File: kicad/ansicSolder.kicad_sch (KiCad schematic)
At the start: 56 parts, among them J1 AudioJack4, J2 AudioJack4, J3 Conn_01x02_Socket, SW1 SW_Push, SW10 SW_Push, SW11 SW_Push, SW12 SW_Push, SW13 SW_Push, SW14 SW_Push, SW15 SW_Push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

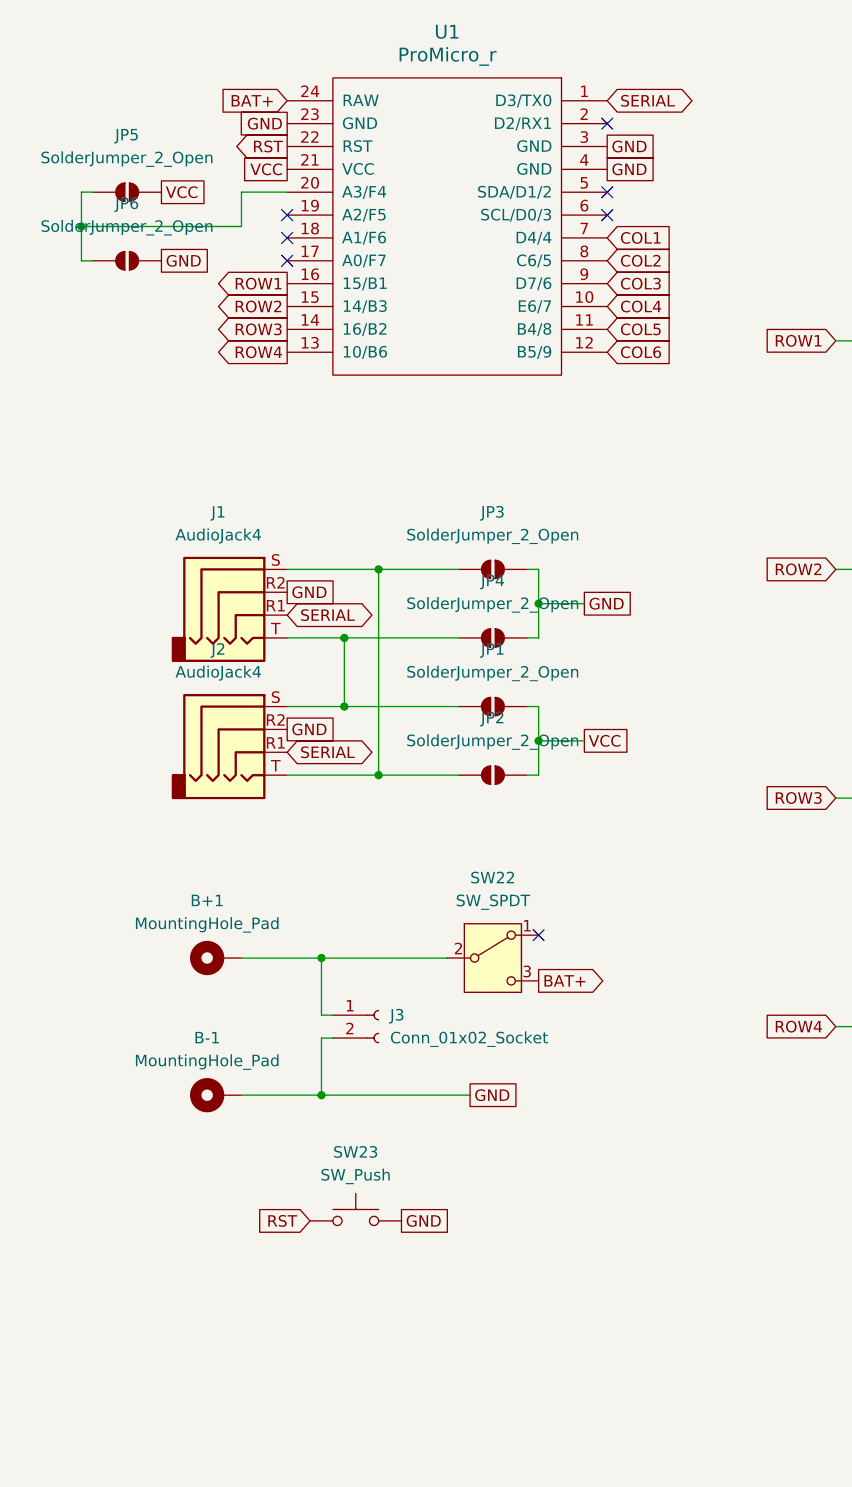
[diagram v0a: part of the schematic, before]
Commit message: edit for more readable schema
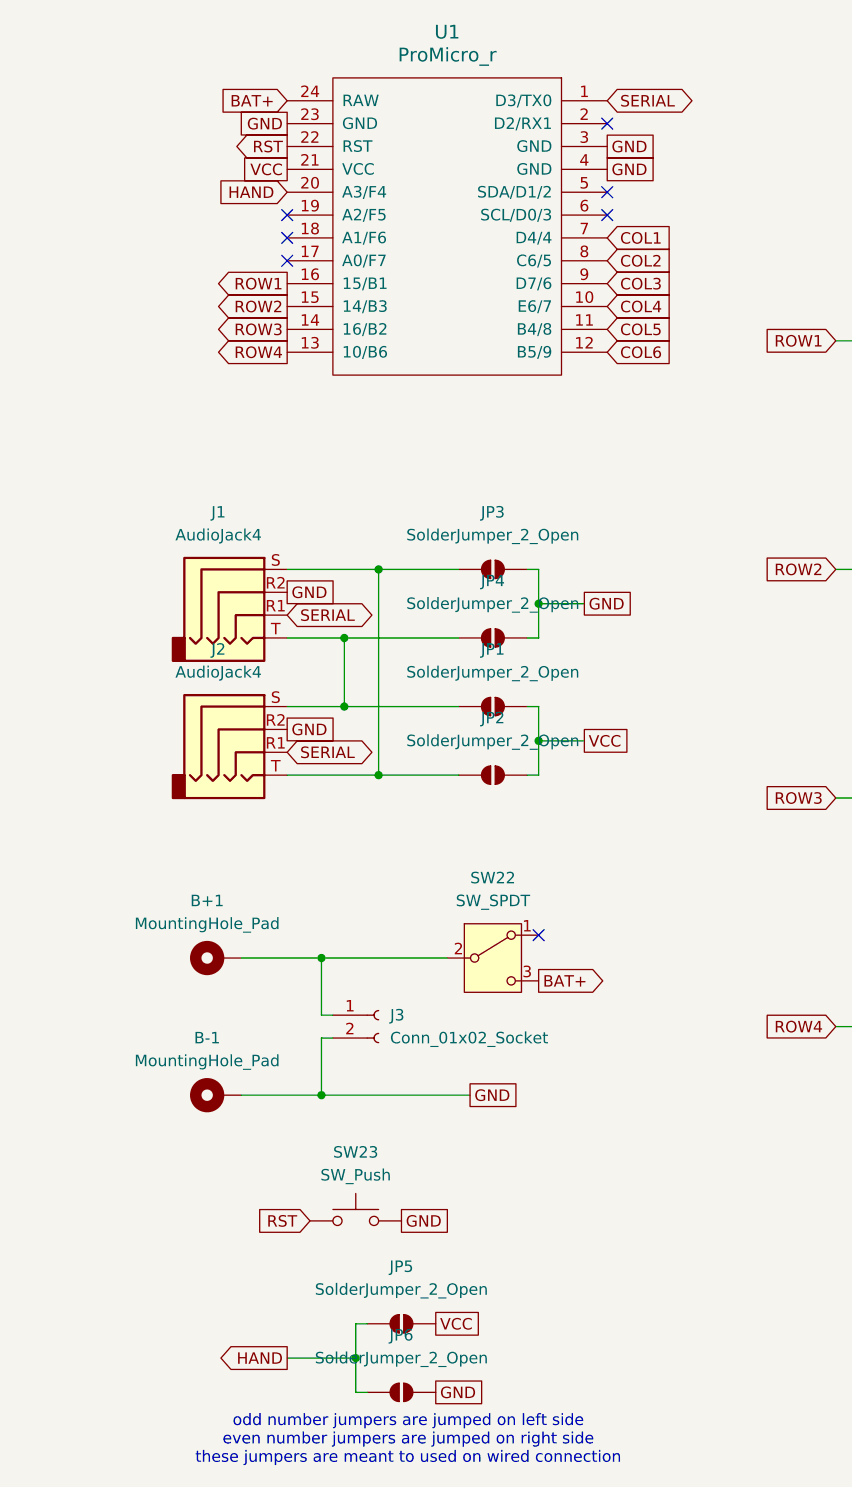
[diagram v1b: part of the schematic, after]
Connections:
- net HAND: now reaches JP5.2 (B), JP6.2 (B), U1.20 (A3/F4)
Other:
- note added: "odd number jumpers are jumped on left side even number jumpers are jumped on right side these jumpers are meant to used on wired connection"
- moved on the sheet: JP5, JP6
